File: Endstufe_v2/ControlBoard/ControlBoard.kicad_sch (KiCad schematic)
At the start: 0 parts

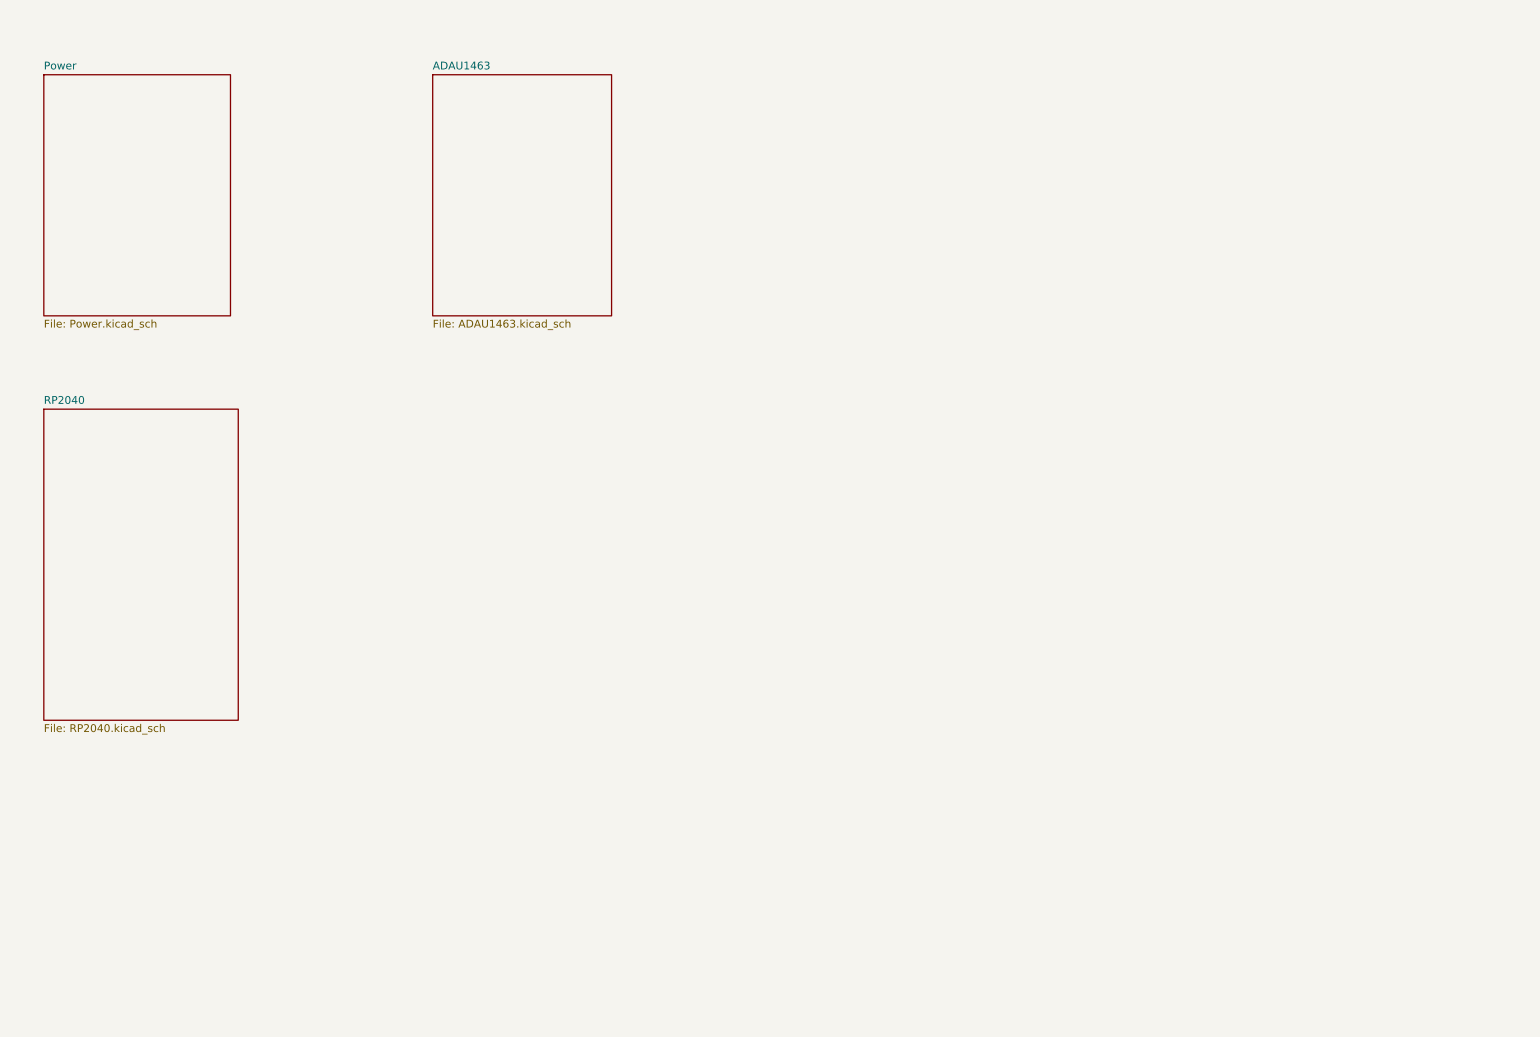
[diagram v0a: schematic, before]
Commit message: Added ADAU1962A DAC schematic
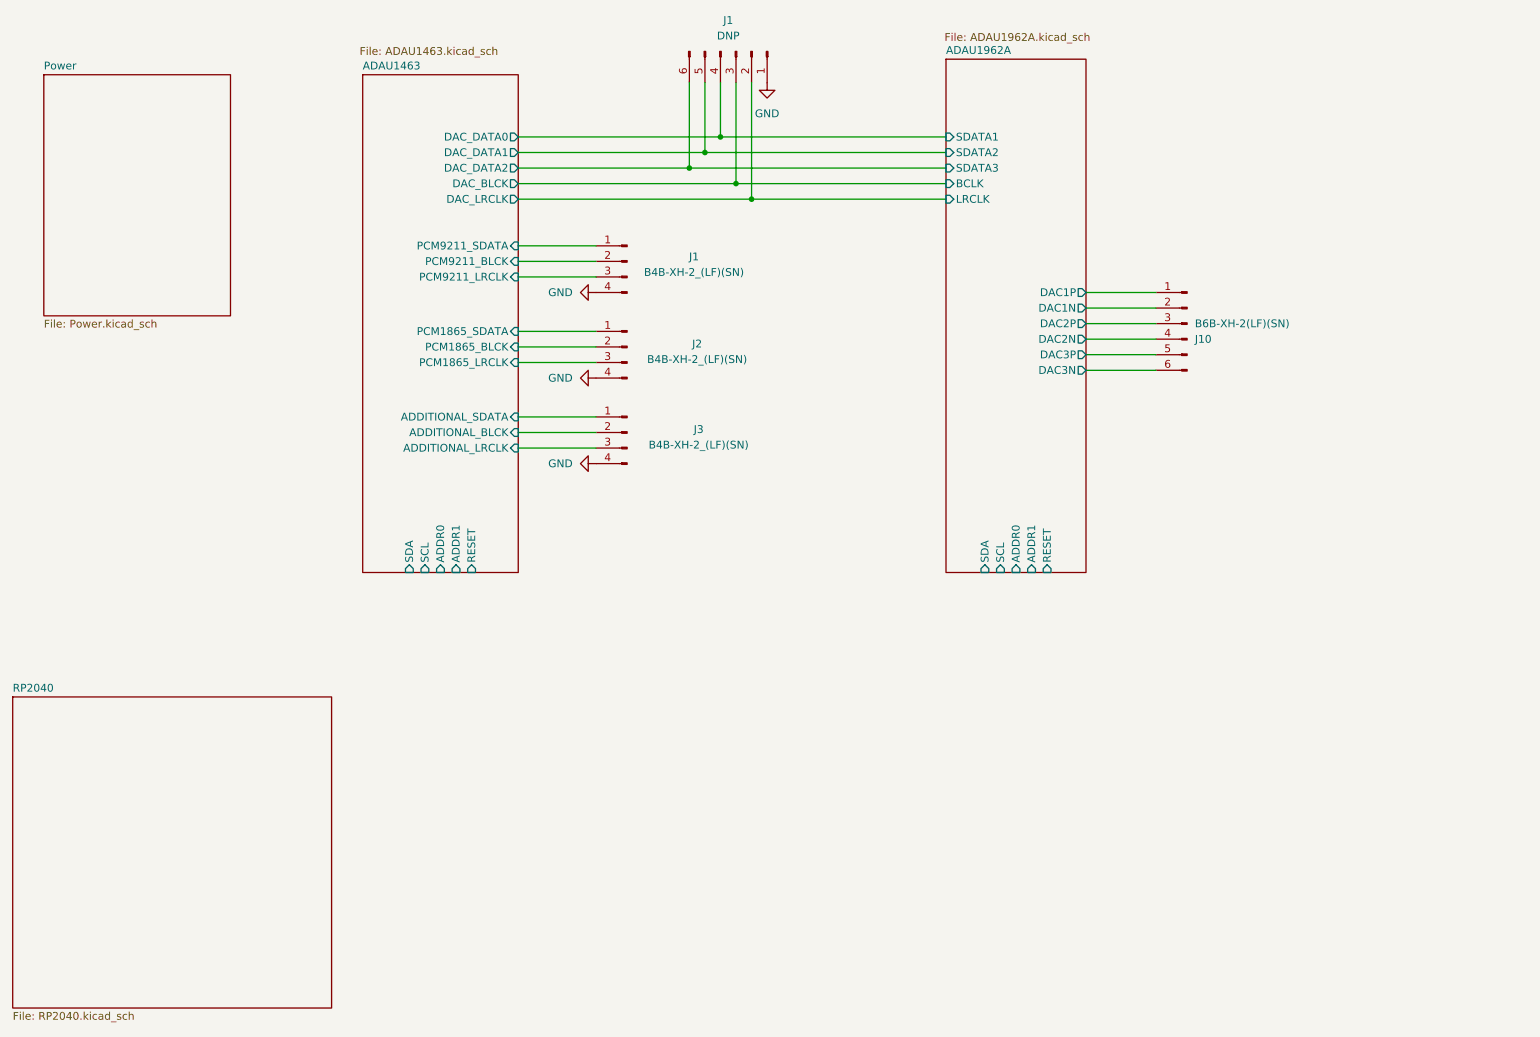
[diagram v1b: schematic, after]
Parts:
- added J1, J2, J3: B4B-XH-2_(LF)(SN), Endstufe:CONN-TH_B4B-XH-2-LF-SN, symbol Connector:Conn_01x04_Pin
- added J1: DNP, symbol Connector:Conn_01x06_Pin
- added J10: B6B-XH-2(LF)(SN), Endstufe:CONN-TH_B6B-XH-2-LF-SN, symbol Connector:Conn_01x06_Pin
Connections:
- new net ADAU1463/ADDITIONAL_BLCK: J3.2 (Pin_2)
- new net ADAU1463/ADDITIONAL_LRCLK: J3.3 (Pin_3)
- new net ADAU1463/ADDITIONAL_SDATA: J3.1 (Pin_1)
- new net ADAU1463/DAC_BLCK: J1.3 (Pin_3)
- new net ADAU1463/DAC_DATA0: J1.4 (Pin_4)
- new net ADAU1463/DAC_DATA1: J1.5 (Pin_5)
- new net ADAU1463/DAC_DATA2: J1.6 (Pin_6)
- new net ADAU1463/DAC_LRCLK: J1.2 (Pin_2)
- new net ADAU1463/PCM1865_BLCK: J2.2 (Pin_2)
- new net ADAU1463/PCM1865_LRCLK: J2.3 (Pin_3)
- new net ADAU1463/PCM1865_SDATA: J2.1 (Pin_1)
- new net ADAU1463/PCM9211_BLCK: J1.2 (Pin_2)
- new net ADAU1463/PCM9211_LRCLK: J1.3 (Pin_3)
- new net ADAU1463/PCM9211_SDATA: J1.1 (Pin_1)
- new net ADAU1962A/DAC1N: J10.2 (Pin_2)
- new net ADAU1962A/DAC1P: J10.1 (Pin_1)
- new net ADAU1962A/DAC2N: J10.4 (Pin_4)
- new net ADAU1962A/DAC2P: J10.3 (Pin_3)
- new net ADAU1962A/DAC3N: J10.6 (Pin_6)
- new net ADAU1962A/DAC3P: J10.5 (Pin_5)
- new net GND: J1.1 (Pin_1), J1.4 (Pin_4), J2.4 (Pin_4), J3.4 (Pin_4)
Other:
- added sheet ADAU1962A (ADAU1962A.kicad_sch)
- sheet ADAU1463 ports: added ADDITIONAL_BLCK, ADDITIONAL_LRCLK, ADDITIONAL_SDATA, ADDR0, ADDR1, DAC_BLCK, DAC_DATA0, DAC_DATA1, DAC_DATA2, DAC_LRCLK, PCM1865_BLCK, PCM1865_LRCLK, PCM1865_SDATA, PCM9211_BLCK, PCM9211_LRCLK, PCM9211_SDATA, RESET, SCL, SDA; removed none

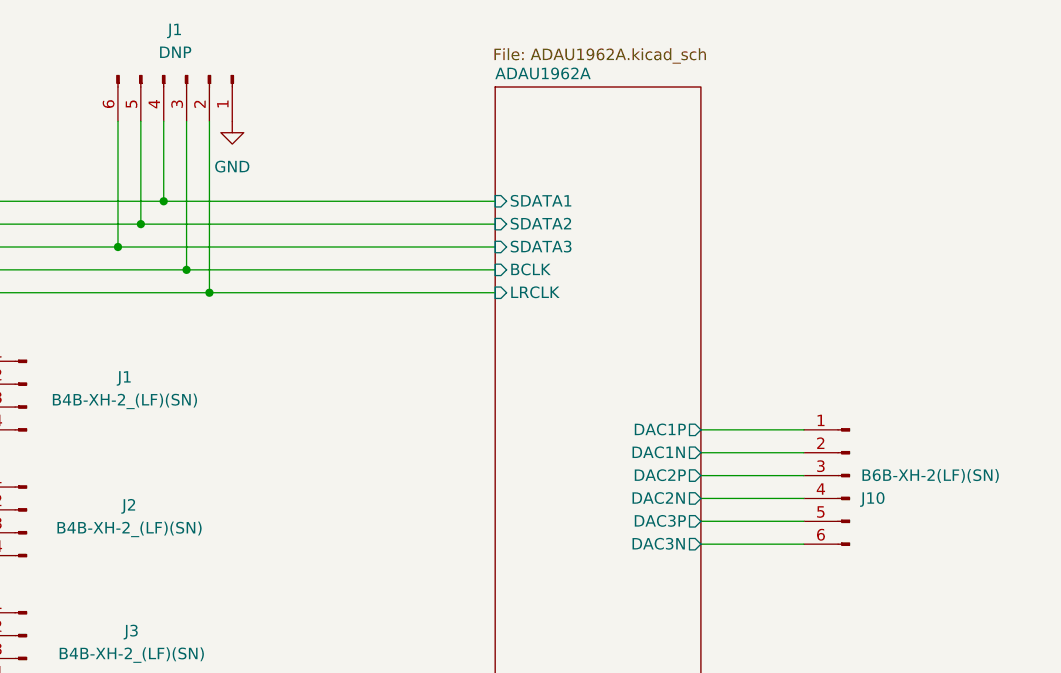
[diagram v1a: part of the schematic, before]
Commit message: Add footprints to all components
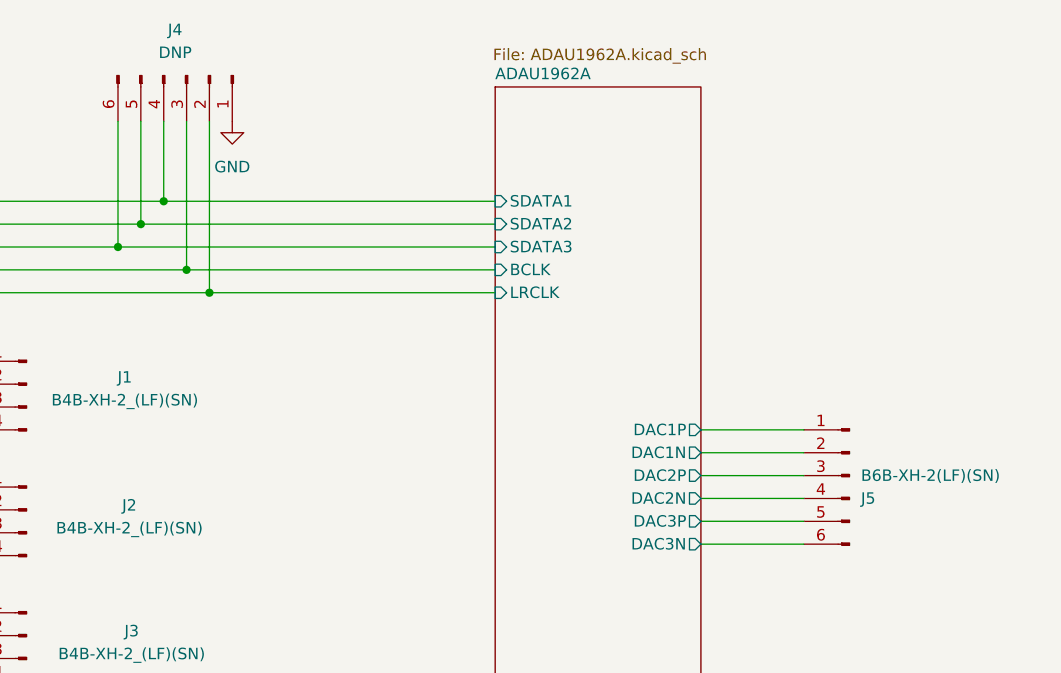
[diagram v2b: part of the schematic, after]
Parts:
- J4: renamed from J1; footprint (none) -> Connector_PinHeader_2.54mm:PinHeader_1x06_P2.54mm_Vertical
- renumbered J10 to J5
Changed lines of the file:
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@@
 		(on_board yes)
 		(dnp no)
-		(property "Reference" "J10"
+		(property "Reference" "J5"
 			(at 218.44 71.1201 0)
 			(effects
@@
 			(project ""
 				(path "/4f887f51-77c1-41d4-a3eb-45d362caffe1"
-					(reference "J10")
+					(reference "J5")
 					(unit 1)
 				)
@@
 		(dnp no)
 		(fields_autoplaced yes)
-		(property "Reference" "J1"
+		(property "Reference" "J4"
 			(at 142.24 19.05 90)
 			(effects
@@
 			)
 		)
-		(property "Footprint" ""
+		(property "Footprint" "Connector_PinHeader_2.54mm:PinHeader_1x06_P2.54mm_Vertical"
 			(at 143.51 24.13 0)
 			(effects
@@
 			(project ""
 				(path "/4f887f51-77c1-41d4-a3eb-45d362caffe1"
-					(reference "J1")
+					(reference "J4")
 					(unit 1)
 				)

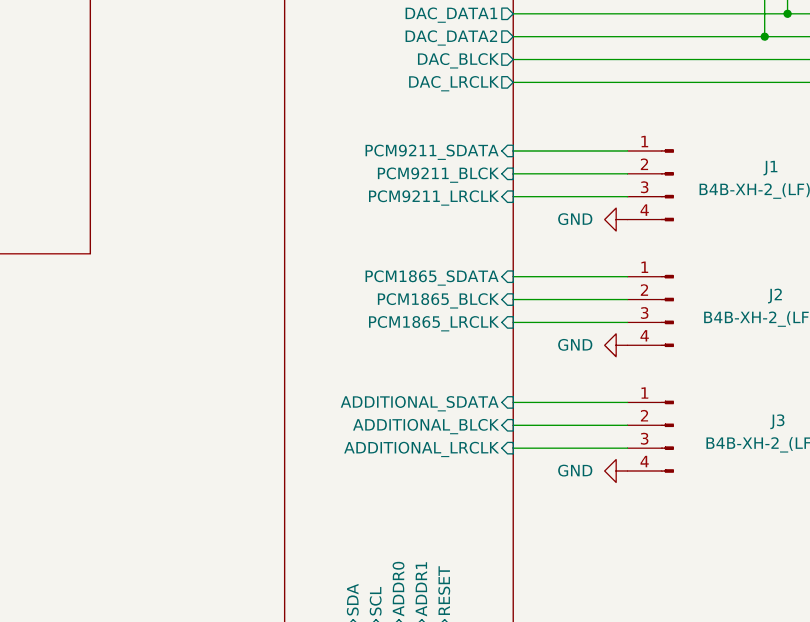
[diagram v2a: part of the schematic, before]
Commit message: Rough layout of components
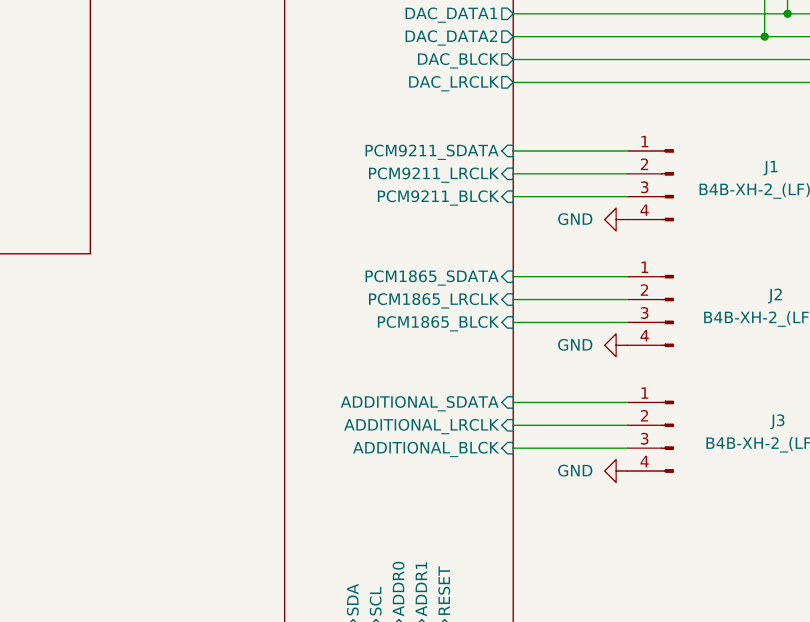
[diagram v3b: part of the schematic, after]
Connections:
- net ADAU1463/ADDITIONAL_BLCK: now also J3.3 (Pin_3); no longer J3.2 (Pin_2)
- net ADAU1463/ADDITIONAL_LRCLK: now also J3.2 (Pin_2); no longer J3.3 (Pin_3)
- net ADAU1463/PCM1865_BLCK: now also J2.3 (Pin_3); no longer J2.2 (Pin_2)
- net ADAU1463/PCM1865_LRCLK: now also J2.2 (Pin_2); no longer J2.3 (Pin_3)
- net ADAU1463/PCM9211_BLCK: now also J1.3 (Pin_3); no longer J1.2 (Pin_2)
- net ADAU1463/PCM9211_LRCLK: now also J1.2 (Pin_2); no longer J1.3 (Pin_3)
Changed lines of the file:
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@@
+	(wire
+		(pts
+			(xy 107.95 58.42) (xy 120.65 58.42)
+		)
+		(stroke
+			(width 0)
+			(type default)
+		)
+	)
+	(wire
+		(pts
+			(xy 200.66 71.12) (xy 212.09 71.12)
+		)
+		(stroke
+			(width 0)
+			(type default)
+		)
+	)
+	(wire
+		(pts
+			(xy 140.97 38.1) (xy 177.8 38.1)
+		)
+		(stroke
+			(width 0)
+			(type default)
+		)
+	)
+	(wire
+		(pts
+			(xy 107.95 60.96) (xy 120.65 60.96)
+		)
+		(stroke
+			(width 0)
+			(type default)
+		)
+	)
+	(wire
+		(pts
+			(xy 107.95 72.39) (xy 120.65 72.39)
+		)
+		(stroke
+			(width 0)
+			(type default)
+		)
+	)
+	(wire
+		(pts
+			(xy 107.95 83.82) (xy 120.65 83.82)
+		)
+		(stroke
+			(width 0)
+			(type default)
+		)
+	)
+	(wire
+		(pts
+			(xy 200.66 76.2) (xy 212.09 76.2)
+		)
+		(stroke
+			(width 0)
+			(type default)
+		)
+	)
+	(wire
+		(pts
+			(xy 107.95 86.36) (xy 120.65 86.36)
+		)
+		(stroke
+			(width 0)
+			(type default)
+		)
+	)
+	(wire
+		(pts
+			(xy 107.95 55.88) (xy 120.65 55.88)
+		)
+		(stroke
+			(width 0)
+			(type default)
+		)
+	)
+	(wire
+		(pts
+			(xy 107.95 45.72) (xy 143.51 45.72)
+		)
+		(stroke
+			(width 0)
+			(type default)
+		)
+	)
+	(wire
+		(pts
+			(xy 143.51 45.72) (xy 143.51 29.21)
+		)
+		(stroke
+			(width 0)
+			(type default)
+		)
+	)
+	(wire
+		(pts
+			(xy 143.51 45.72) (xy 177.8 45.72)
+		)
+		(stroke
+			(width 0)
+			(type default)
+		)
+	)
+	(wire
+		(pts
+			(xy 200.66 68.58) (xy 212.09 68.58)
+		)
+		(stroke
+			(width 0)
+			(type default)
+		)
+	)
+	(wire
+		(pts
+			(xy 107.95 40.64) (xy 138.43 40.64)
+		)
+		(stroke
+			(width 0)
+			(type default)
+		)
+	)
+	(wire
+		(pts
+			(xy 140.97 38.1) (xy 140.97 29.21)
+		)
+		(stroke
+			(width 0)
+			(type default)
+		)
+	)
+	(wire
+		(pts
+			(xy 146.05 48.26) (xy 177.8 48.26)
+		)
+		(stroke
+			(width 0)
+			(type default)
+		)
+	)
+	(wire
+		(pts
+			(xy 200.66 73.66) (xy 212.09 73.66)
+		)
+		(stroke
+			(width 0)
+			(type default)
+		)
+	)
+	(wire
+		(pts
+			(xy 146.05 48.26) (xy 146.05 29.21)
+		)
+		(stroke
+			(width 0)
+			(type default)
+		)
+	)
 	(wire
 		(pts
@@
 	(wire
 		(pts
-			(xy 200.66 71.12) (xy 212.09 71.12)
-		)
-		(stroke
-			(width 0)
-			(type default)
-		)
-	)
-	(wire
-		(pts
-			(xy 140.97 38.1) (xy 177.8 38.1)
-		)
-		(stroke
-			(width 0)
-			(type default)
-		)
-	)
-	(wire
-		(pts
-			(xy 107.95 72.39) (xy 120.65 72.39)
-		)
-		(stroke
-			(width 0)
-			(type default)
-		)
-	)
-	(wire
-		(pts
-			(xy 107.95 83.82) (xy 120.65 83.82)
-		)
-		(stroke
-			(width 0)
-			(type default)
-		)
-	)
-	(wire
-		(pts
-			(xy 200.66 76.2) (xy 212.09 76.2)
-		)
-		(stroke
-			(width 0)
-			(type default)
-		)
-	)
-	(wire
-		(pts
-			(xy 107.95 55.88) (xy 120.65 55.88)
-		)
-		(stroke
-			(width 0)
-			(type default)
-		)
-	)
-	(wire
-		(pts
-			(xy 107.95 45.72) (xy 143.51 45.72)
-		)
-		(stroke
-			(width 0)
-			(type default)
-		)
-	)
-	(wire
-		(pts
-			(xy 107.95 86.36) (xy 120.65 86.36)
-		)
-		(stroke
-			(width 0)
-			(type default)
-		)
-	)
-	(wire
-		(pts
-			(xy 143.51 45.72) (xy 143.51 29.21)
-		)
-		(stroke
-			(width 0)
-			(type default)
-		)
-	)
-	(wire
-		(pts
-			(xy 143.51 45.72) (xy 177.8 45.72)
-		)
-		(stroke
-			(width 0)
-			(type default)
-		)
-	)
-	(wire
-		(pts
-			(xy 200.66 68.58) (xy 212.09 68.58)
-		)
-		(stroke
-			(width 0)
-			(type default)
-		)
-	)
-	(wire
-		(pts
-			(xy 107.95 40.64) (xy 138.43 40.64)
-		)
-		(stroke
-			(width 0)
-			(type default)
-		)
-	)
-	(wire
-		(pts
-			(xy 140.97 38.1) (xy 140.97 29.21)
-		)
-		(stroke
-			(width 0)
-			(type default)
-		)
-	)
-	(wire
-		(pts
-			(xy 146.05 48.26) (xy 177.8 48.26)
-		)
-		(stroke
-			(width 0)
-			(type default)
-		)
-	)
-	(wire
-		(pts
-			(xy 107.95 58.42) (xy 120.65 58.42)
-		)
-		(stroke
-			(width 0)
-			(type default)
-		)
-	)
-	(wire
-		(pts
-			(xy 200.66 73.66) (xy 212.09 73.66)
-		)
-		(stroke
-			(width 0)
-			(type default)
-		)
-	)
-	(wire
-		(pts
-			(xy 107.95 60.96) (xy 120.65 60.96)
-		)
-		(stroke
-			(width 0)
-			(type default)
-		)
-	)
-	(wire
-		(pts
-			(xy 146.05 48.26) (xy 146.05 29.21)
+			(xy 107.95 48.26) (xy 146.05 48.26)
 		)
 		(stroke
@@
 		(pts
 			(xy 107.95 74.93) (xy 120.65 74.93)
-		)
-		(stroke
-			(width 0)
-			(type default)
-		)
-	)
-	(wire
-		(pts
-			(xy 107.95 48.26) (xy 146.05 48.26)
 		)
 		(stroke
@@
 		)
 		(pin "PCM1865_BLCK" input
+			(at 107.95 74.93 0)
+			(effects
+				(font
+					(size 1.27 1.27)
+				)
+				(justify right)
+			)
+		)
+		(pin "PCM1865_LRCLK" input
 			(at 107.95 72.39 0)
 			(effects
@@
 			)
 		)
-		(pin "PCM1865_LRCLK" input
-			(at 107.95 74.93 0)
-			(effects
-				(font
-					(size 1.27 1.27)
-				)
-				(justify right)
-			)
-		)
 		(pin "PCM9211_BLCK" input
+			(at 107.95 60.96 0)
+			(effects
+				(font
+					(size 1.27 1.27)
+				)
+				(justify right)
+			)
+		)
+		(pin "PCM9211_LRCLK" input
 			(at 107.95 58.42 0)
-			(effects
-				(font
-					(size 1.27 1.27)
-				)
-				(justify right)
-			)
-		)
-		(pin "PCM9211_LRCLK" input
-			(at 107.95 60.96 0)
 			(effects
 				(font
@@
 		)
 		(pin "ADDITIONAL_LRCLK" input
+			(at 107.95 86.36 0)
+			(effects
+				(font
+					(size 1.27 1.27)
+				)
+				(justify right)
+			)
+		)
+		(pin "ADDITIONAL_BLCK" input
 			(at 107.95 88.9 0)
 			(effects
 				(font
-					(size 1.27 1.27)
-				)
-				(justify right)
-			)
-		)
-		(pin "ADDITIONAL_BLCK" input
-			(at 107.95 86.36 0)
-			(effects
-				(font

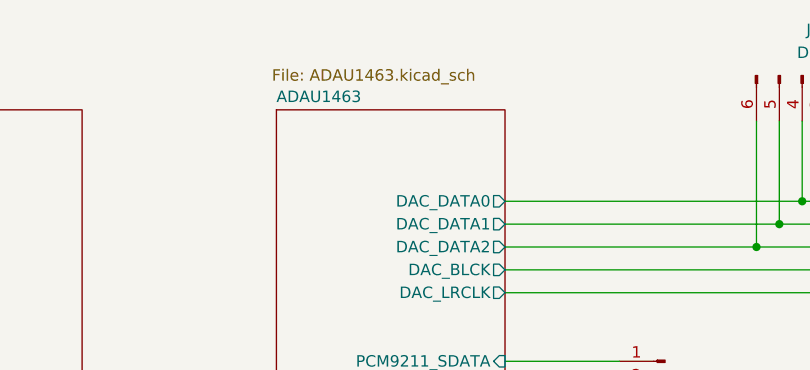
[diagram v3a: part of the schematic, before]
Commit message: Continue working on input board and use ADAU1467 instaed of ADAU1463
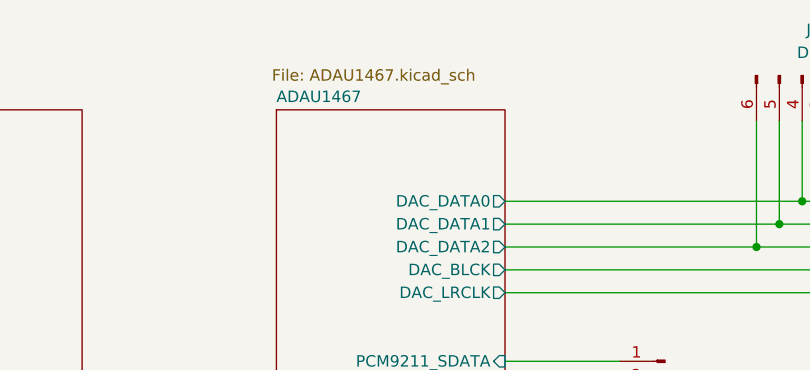
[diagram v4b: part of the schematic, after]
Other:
- sheet ADAU1463 renamed ADAU1467
- sheet ADAU1467: file ADAU1463.kicad_sch -> ADAU1467.kicad_sch
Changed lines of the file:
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@@
 			(color 0 0 0 0.0000)
 		)
-		(property "Sheetname" "ADAU1463"
+		(property "Sheetname" "ADAU1467"
 			(at 82.55 27.2284 0)
 			(effects
@@
 			)
 		)
-		(property "Sheetfile" "ADAU1463.kicad_sch"
+		(property "Sheetfile" "ADAU1467.kicad_sch"
 			(at 82.042 23.368 0)
 			(effects

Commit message: Continue layouting
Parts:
- added J15: B4B-XH-2_(LF)(SN), Endstufe:CONN-TH_B4B-XH-2-LF-SN, symbol Connector:Conn_01x04_Pin
- added J16: B6B-XH-2(LF)(SN), Endstufe:CONN-TH_B6B-XH-2-LF-SN, symbol Connector:Conn_01x06_Pin
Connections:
- net GND: now also J15.2 (Pin_2)
- new net FAULTZA: J16.3 (Pin_3)
- new net FAULTZB: J16.4 (Pin_4)
- new net MUTEA: J16.5 (Pin_5)
- new net MUTEB: J16.6 (Pin_6)
- new net PCM9211_RST: J15.1 (Pin_1)
- new net SCL: J15.3 (Pin_3)
- new net SDA: J15.4 (Pin_4)
- new net SDZA: J16.1 (Pin_1)
- new net SDZB: J16.2 (Pin_2)
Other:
- sheet RP2040 ports: added GPIO0_I2C0_SDA, GPIO10, GPIO1_I2C0_SCL, GPIO2, GPIO3, GPIO4, GPIO5, GPIO6, GPIO7, GPIO8, GPIO9; removed none
